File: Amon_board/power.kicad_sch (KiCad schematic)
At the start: 37 parts, among them J3 Switch_port, J4 XT60-F, J5 XT60-F, U4 MP2303ADN, U5 MP2303ADN

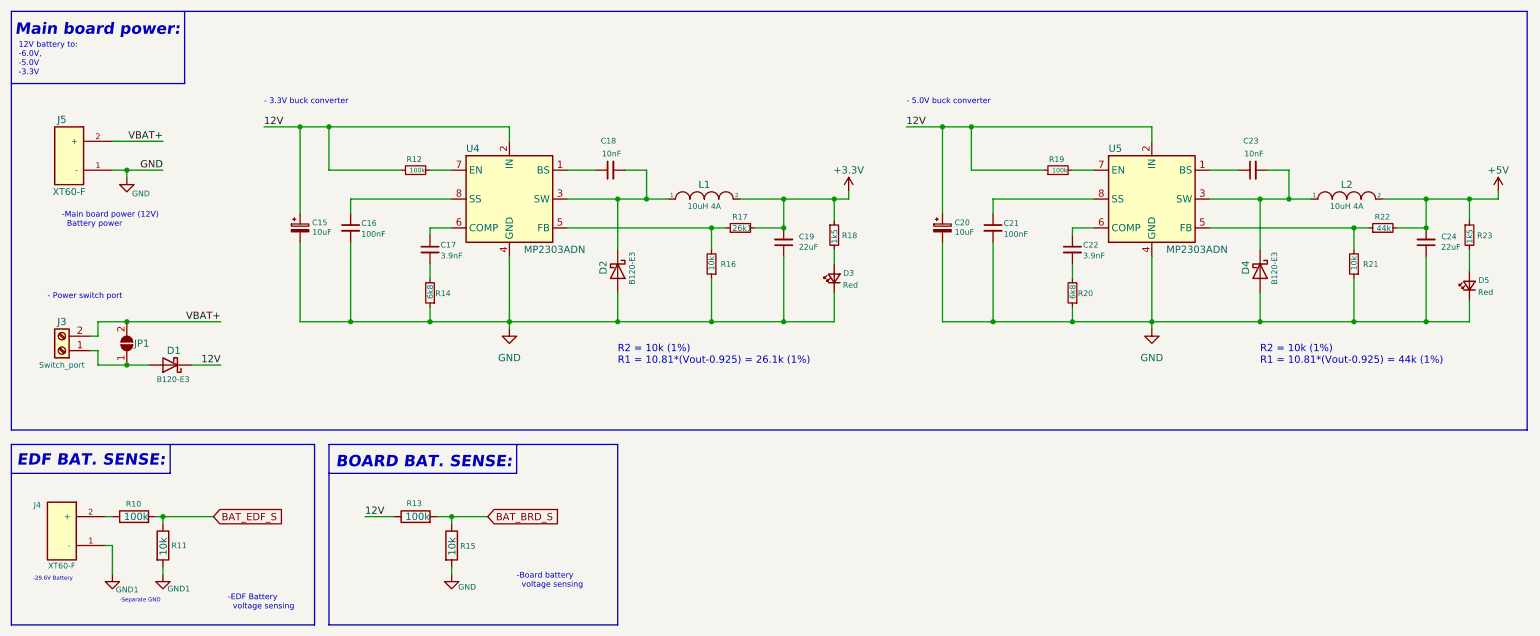
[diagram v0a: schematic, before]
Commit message: PCB update, stl update (pcb holder)
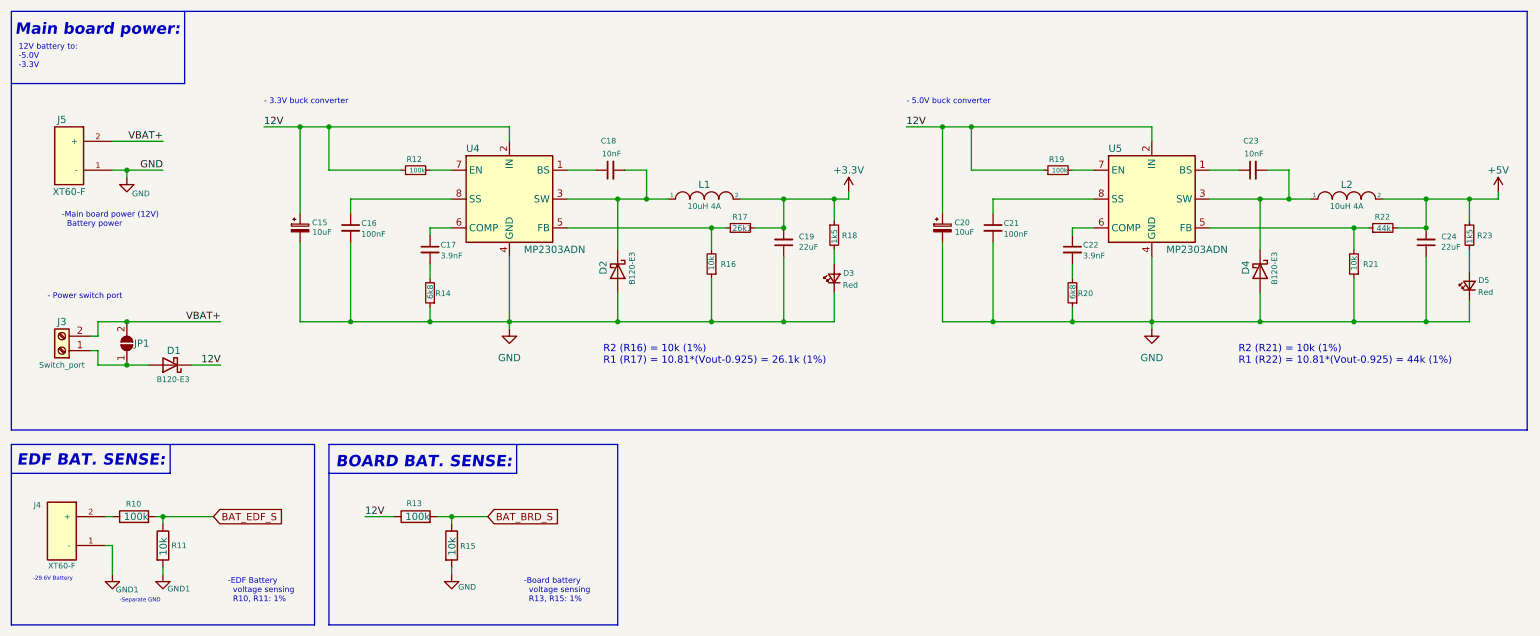
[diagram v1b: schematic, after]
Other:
- note added: "-Board battery voltage sensing R13, R15: 1%"
- note added: "-EDF Battery voltage sensing R10, R11: 1%"
- note added: "12V battery to: -5.0V -3.3V"
- note added: "R2 (R16) = 10k (1%) R1 (R17) = 10.81*(Vout-0.925) = 26.1k (1%)"
- note added: "R2 (R21) = 10k (1%) R1 (R22) = 10.81*(Vout-0.925) = 44k (1%)"
- note removed: "-Board battery voltage sensing"
- note removed: "-EDF Battery voltage sensing"
- note removed: "12V battery to: -6.0V, -5.0V -3.3V"
- note removed: "R2 = 10k (1%) R1 = 10.81*(Vout-0.925) = 26.1k (1%)"
- note removed: "R2 = 10k (1%) R1 = 10.81*(Vout-0.925) = 44k (1%)"
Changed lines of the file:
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@@
   (title_block
     (title "Amon Board - Power")
-    (date "2022-10-19")
-    (rev "2.0")
+    (date "2023-02-15")
+    (rev "2.2")
     (company "Tinta T.")
   )
@@
     (stroke (width 0) (type default) (color 0 0 0 0))
   )
-  (text "-Board battery \n  voltage sensing" (at 104.14 116.84 0)
+  (text "-Board battery \n  voltage sensing\n  R13, R15: 1%" (at 105.41 119.38 0)
     (effects (font (size 1 1)) (justify left bottom))
   )
@@
     (effects (font (size 0.7 0.7)) (justify left bottom))
   )
-  (text "-EDF Battery \n  voltage sensing\n" (at 53.34 120.65 0)
-    (effects (font (size 1 1)) (justify left bottom))
-  )
-  (text "12V battery to:\n-6.0V,\n-5.0V\n-3.3V" (at 16.51 26.67 0)
+  (text "-EDF Battery \n  voltage sensing\n  R10, R11: 1%" (at 53.34 119.38 0)
+    (effects (font (size 1 1)) (justify left bottom))
+  )
+  (text "12V battery to:\n-5.0V\n-3.3V" (at 16.51 25.4 0)
     (effects (font (size 1 1)) (justify left bottom))
   )
@@
     (effects (font (size 2 2) (thickness 0.4) bold italic) (justify left bottom))
   )
-  (text "R2 = 10k (1%)\nR1 = 10.81*(Vout-0.925) = 44k (1%)" (at 234.95 77.47 0)
+  (text "R2 (R21) = 10k (1%)\nR1 (R22) = 10.81*(Vout-0.925) = 44k (1%)"
+    (at 231.14 77.47 0)
     (effects (font (size 1.27 1.27)) (justify left bottom))
   )
@@
     (effects (font (size 2 2) (thickness 0.4) bold italic) (justify left bottom))
   )
-  (text "R2 = 10k (1%)\nR1 = 10.81*(Vout-0.925) = 26.1k (1%)"
-    (at 121.92 77.47 0)
+  (text "R2 (R16) = 10k (1%)\nR1 (R17) = 10.81*(Vout-0.925) = 26.1k (1%)"
+    (at 119.38 77.47 0)
     (effects (font (size 1.27 1.27)) (justify left bottom))
   )

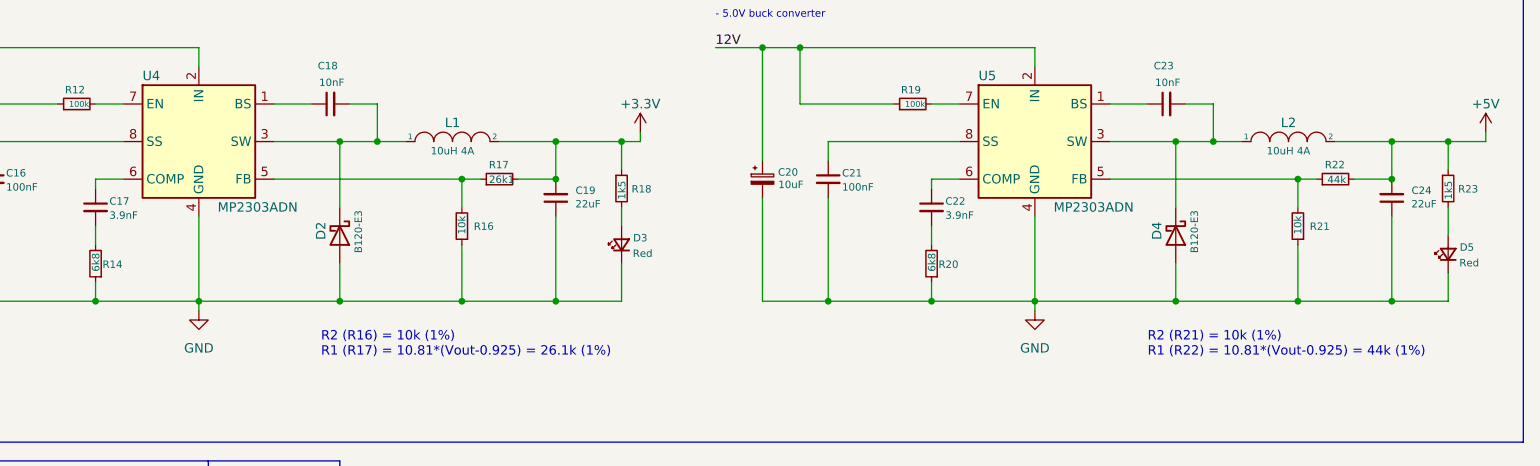
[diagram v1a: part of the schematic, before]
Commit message: PCB repair: crystal footprint, radio connector fliped, text
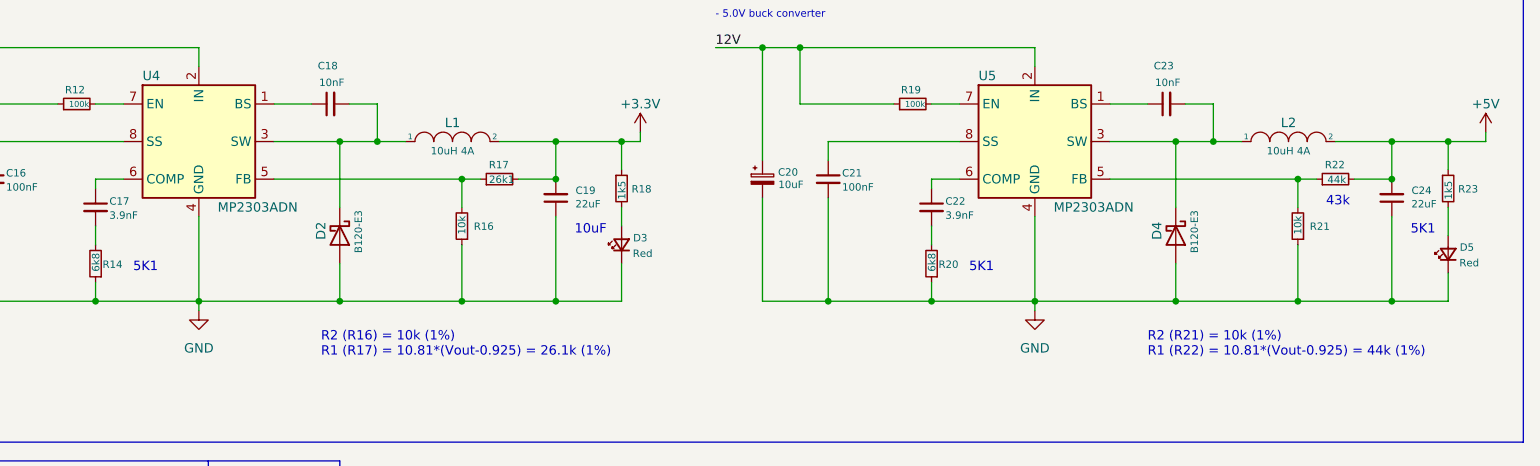
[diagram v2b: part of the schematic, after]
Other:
- note added: "10uF"
- note added: "43k"
- note added: "5K1"
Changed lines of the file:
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@@
     (effects (font (size 1 1)) (justify left bottom))
+  )
+  (text "5K1" (at 266.7 60.96 0)
+    (effects (font (size 1.27 1.27)) (justify left bottom))
   )
   (text "-Separate GND" (at 34.29 119.38 0)
@@
   (text "-Main board power (12V) \n  Battery power" (at 24.13 53.34 0)
     (effects (font (size 1 1)) (justify left bottom))
+  )
+  (text "5K1" (at 207.01 66.04 0)
+    (effects (font (size 1.27 1.27)) (justify left bottom))
   )
   (text "- 5.0V buck converter" (at 172.72 31.75 0)
@@
     (effects (font (size 1.27 1.27)) (justify left bottom))
   )
+  (text "10uF" (at 153.67 60.96 0)
+    (effects (font (size 1.27 1.27)) (justify left bottom))
+  )
+  (text "43k" (at 255.27 57.15 0)
+    (effects (font (size 1.27 1.27)) (justify left bottom))
+  )
+  (text "5K1" (at 93.98 66.04 0)
+    (effects (font (size 1.27 1.27)) (justify left bottom))
+  )

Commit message: changed directories
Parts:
- C19, C24: footprint Capacitor_SMD:C_0603_1608Metric -> Capacitor_SMD:C_1206_3216Metric
- J4, J5: footprint XT60-M:AMASS_XT60-M -> XT60:AMASS_XT60-M
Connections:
- no-connect marks 0 -> 1
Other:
- note added: "5k1"
- note added: "5k1||5k1"
- note removed: "10uF"
- note removed: "5K1"
